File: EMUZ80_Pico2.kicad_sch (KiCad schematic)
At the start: 16 parts, among them J1 Conn_01x20_Socket, J2 Conn_01x20_Socket, SW1 SW_Push, SW2 SW_Push, U1 Pimoroni PGA2350B, U2 RB2350B_Core_Board, U3 74HC00, U4 Z80CPU, U5 HM628128_DIP32_SOP32

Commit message: schematic finished
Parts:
- removed J1, J2: Conn_01x20_Socket, Connector_PinSocket_2.54mm:PinSocket_1x20_P2.54mm_Vertical, symbol kuma-lib1:Conn_01x20_Socket
- removed U3: 74HC00, Package_DIP:DIP-14_W7.62mm_Socket, symbol kuma-lib1:74HC00
- added C1, C2: 0.1u, symbol Device:C_Small
- added C3, C4, C5, C6: C_Small, symbol Device:C_Small
- added D5: D_Schottky_Small, symbol local:D_Schottky_Small
- added J1: Z80_L, symbol local:Conn_01x20_Socket
- added J2: Z80_R, symbol local:Conn_01x20_Socket
- added J3: EXT_GPIO1, symbol Connector:Conn_01x08_Pin
- added J4: EXT_GPIO2, symbol Connector:Conn_01x02_Pin
- added J5: Serial, symbol Connector:Conn_01x06_Pin
- added J6: USB_B_Micro, symbol Connector:USB_B_Micro
- added J8: Conn_01x05_Pin, symbol Connector:Conn_01x05_Pin
- added JP1: VCC_Jumper, symbol Jumper:Jumper_2_Small_Bridged
- added U3: 74HC00, symbol local:74HC00
- D2: value LED_Small -> RED; footprint kuma-f:LED_D3.0mm -> local-f:LED_D3.0mm
- D3: value LED_Small -> GREEN; footprint kuma-f:LED_D3.0mm -> local-f:LED_D3.0mm
- D4: value LED_Small -> YELLOW; footprint kuma-f:LED_D3.0mm -> local-f:LED_D3.0mm
- R1, R2, R3: value R_Small -> 1k; footprint kuma-f:R_Axial_DIN0207_L6.3mm_D2.5mm_P7.62mm_Horizontal -> local-f:R_Axial_DIN0207_L6.3mm_D2.5mm_P7.62mm_Horizontal
- SW1: value SW_Push -> RUN; footprint kuma-f:Tact_SW -> local-f:Tact_SW
- SW2: value SW_Push -> BOOTSEL; footprint kuma-f:Tact_SW -> local-f:Tact_SW
- U2: footprint local-f:RB2350B_Core_Board -> (none)
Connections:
- net A0: now also J2.11 (Pin_11)
- net A1: now also J2.10 (Pin_10)
- net A10: now also J2.1 (Pin_1)
- net A11: now also J1.1 (Pin_1)
- net A12: now also J1.2 (Pin_2)
- net A13: now also J1.3 (Pin_3)
- net A14: now also J1.4 (Pin_4)
- net A15: now also J1.5 (Pin_5)
- net A2: now also J2.9 (Pin_9)
- net A3: now also J2.8 (Pin_8)
- net A4: now also J2.7 (Pin_7)
- net A5: now also J2.6 (Pin_6)
- net A6: now also J2.5 (Pin_5)
- net A7: now also J2.4 (Pin_4)
- net A8: now also J2.3 (Pin_3)
- net A9: now also J2.2 (Pin_2)
- net BUSAK: now also U1.I8 (GPIO29), U2.R25 (GPIO29), J2.18 (Pin_18)
- net BUSRQ: now also U1.C9 (GPIO43_ADC3), U2.R11 (GPIO43_ADC3), J2.16 (Pin_16)
- net CLK: now also J1.6 (Pin_6), U3.11
- net D0: now also J1.14 (Pin_14)
- net D1: now also J1.15 (Pin_15)
- net D2: now also J1.12 (Pin_12)
- net D3: now also J1.8 (Pin_8)
- net D4: now also J1.7 (Pin_7)
- net D5: now also J1.9 (Pin_9)
- net D6: now also J1.10 (Pin_10)
- net D7: now also J1.13 (Pin_13)
- net GND: now also R1.2, SW1.1, SW2.1, U1.A1 (GND), U1.A10 (GND), U1.B2 (GND), U1.B9 (GND), U1.J1 (GND), U1.J10 (GND), U2.L3 (GND), U2.L4 (GND), U2.R1 (GND), U2.R2 (GND), U2.R4 (GND), C1.2, C2.2, C3.2, C4.2, C5.2, C6.2, J2.12 (Pin_12), J5.6 (Pin_6), J6.5 (GND), J6.6 (Shield), J8.5 (Pin_5), U3.7 (GND)
- net HALT: now also R3.2, J1.18 (Pin_18)
- net INT: now also J1.16 (Pin_16), U3.3
- net IORQ: now also U1.J6 (GPIO24), U2.L30 (GPIO24), J1.20 (Pin_20)
- net M1: now also U1.I7 (GPIO27), U2.R27 (GPIO27), J2.14 (Pin_14)
- net MREQ: now also U1.I6 (GPIO25), U2.R29 (GPIO25), J1.19 (Pin_19)
- net NMI: now also J1.17 (Pin_17)
- net RD: now also U1.J7 (GPIO26), U2.R30 (GPIO26), J2.20 (Pin_20)
- net RESET: now also R2.2, U1.D10 (GPIO42_ADC2), U2.R14 (GPIO42_ADC2), J2.15 (Pin_15)
- net RFSH: now also U1.J8 (GPIO28), U2.R28 (GPIO28), J2.13 (Pin_13)
- net VCC: now also D2.2 (A), D3.2 (A), D4.2 (A), U4.11 (VCC), U5.32 (VCC), C1.1, C2.1, J1.11 (Pin_11), JP1.2 (B), U3.13, U3.14 (VCC), U3.2
- net WAIT: now also U1.I9 (GPIO31), U2.R23 (GPIO31), J2.17 (Pin_17)
- net WR: now also U1.J9 (GPIO30), U2.R26 (GPIO30), J2.19 (Pin_19)
- net +5V: now reaches D1.1 (K)
- net +5V: now also U1.A3 (VBUS), C3.1, C4.1, C5.1, C6.1, D5.1 (K), JP1.1 (A)
- net at D1.2 (A): now also J6.1 (VBUS), J8.1 (Pin_1)
- net at D3.1 (K): now also R2.1
- net at R1.1: now also D2.1 (K)
- net RAMCS: now reaches U5.30 (CS2/CE2)
- net RAMCS: now also U1.C10 (GPIO44_ADC4), U2.R12 (GPIO44_ADC4), J4.1 (Pin_1)
- net at D4.1 (K): now also R3.1
- net at U2.L1 (VBUS): now also D5.2 (A)
- net RX: now reaches U2.R10 (GPIO46_ADC6)
- net RX: now also U1.A9 (GPIO46_ADC6), J5.2 (Pin_2)
- net GPIO41: now reaches U2.R13 (GPIO41_ADC1)
- net GPIO41: now also U1.D9 (GPIO41_ADC1), U3.1
- net GPIO39: now reaches U2.R15 (GPIO39)
- net GPIO39: now also U1.E9 (GPIO39), J3.8 (Pin_8)
- net GPIO40: now reaches U2.R16 (GPIO40_ADC0)
- net GPIO40: now also U1.E10 (GPIO40_ADC0), U3.12
- net GPIO37: now reaches U2.R17 (GPIO37)
- net GPIO37: now also U1.F9 (GPIO37), J3.6 (Pin_6)
- net GPIO38: now reaches U2.R18 (GPIO38)
- net GPIO38: now also U1.F10 (GPIO38), J3.7 (Pin_7)
- net GPIO35: now reaches U2.R19 (GPIO35)
- net GPIO35: now also U1.G9 (GPIO35), J3.4 (Pin_4)
- net GPIO36: now reaches U2.R20 (GPIO36)
- net GPIO36: now also U1.G10 (GPIO36), J3.5 (Pin_5)
- net GPIO33: now reaches U2.R21 (GPIO33)
- net GPIO33: now also U1.H9 (GPIO33), J3.2 (Pin_2)
- net GPIO34: now reaches U2.R22 (GPIO34)
- net GPIO34: now also U1.H10 (GPIO34), J3.3 (Pin_3)
- net GPIO32: now reaches U2.R24 (GPIO32)
- net GPIO32: now also U1.I10 (GPIO32), J3.1 (Pin_1)
- net TX: now reaches U2.R7 (GPIO47_ADC7)
- net TX: now also U1.B8 (GPIO47_ADC7), J5.3 (Pin_3)
- net GPIO45: now reaches U2.R9 (GPIO45_ADC5)
- net GPIO45: now also U1.B10 (GPIO45_ADC5), J4.2 (Pin_2)
- net at U1.A5 (RUN): now also SW1.2
- net at U1.A6 (USB_DP): now also J6.3 (D+), J8.3 (Pin_3)
- net at U1.A7 (USB_DM): now also J6.2 (D-), J8.2 (Pin_2)
- net at U1.A8 (BOOTSEL): now also SW2.2
- new net CTS: J5.5 (Pin_5)
- new net DTR: J5.1 (Pin_1)
- no-connect marks 0 -> 22
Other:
- note added: "D+"
- note added: "D-"
- note added: "GND"
- note added: "ID"
- note added: "VCC"
- moved on the sheet: D1, D2, D3, D4, R1, R2, R3, SW1, SW2

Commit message: schematic done, pcb now working
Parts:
- removed C6: C_Small, symbol Device:C_Small
- added C7: 10uF, Capacitor_THT:CP_Radial_D5.0mm_P2.50mm, symbol Device:C_Polarized_Small
- C1, C2: footprint (none) -> Capacitor_THT:C_Disc_D3.0mm_W1.6mm_P2.50mm
- C3, C4, C5: value C_Small -> 0.1u; footprint (none) -> Capacitor_THT:C_Disc_D3.0mm_W1.6mm_P2.50mm
- D1, D5: value D_Schottky_Small -> 1S3; footprint (none) -> local-f:D_DO-34_SOD68_P7.62mm_Horizontal
- J1, J2: footprint (none) -> local-f:PinHeader_1x20_P2.54mm_Ovalpad_Vertical
- J3: footprint (none) -> Connector_PinHeader_2.54mm:PinHeader_1x08_P2.54mm_Vertical
- J4: footprint (none) -> Connector_PinHeader_2.54mm:PinHeader_1x02_P2.54mm_Vertical
- J5: footprint (none) -> local-f:PinHeader_1x06_P2.54mm_Horizontal_NoFeet
- J6: footprint (none) -> Connector_USB:USB_Micro-B_Amphenol_10103594-0001LF_Horizontal
- J8: footprint (none) -> Connector_PinHeader_2.54mm:PinHeader_1x05_P2.54mm_Vertical
- JP1: footprint (none) -> Jumper:SolderJumper-2_P1.3mm_Bridged_RoundedPad1.0x1.5mm
- R1, R2, R3: footprint local-f:R_Axial_DIN0207_L6.3mm_D2.5mm_P7.62mm_Horizontal -> local-f:R_Axial_L5.5mm_D2.0mm_P7.62mm_Horizontal
- U2: footprint (none) -> local-f:RB2350B_Core_Board
- U3: footprint (none) -> Package_DIP:DIP-14_W7.62mm_Socket
- U4: footprint Package_DIP:DIP-40_W15.24mm_Socket -> local-f:DIP-40_W15.24mm_Socket_OvalPad_splitcouryard
- U5: value HM628128_DIP32_SOP32 -> HM628128
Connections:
- net +5V: now also D2.2 (A), C7.1; no longer C3.1
- net GND: now also C7.2; no longer C3.2
- net VCC: now also C3.1; no longer D2.2 (A)
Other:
- moved on the sheet: C3, C4, C5, D2, R1

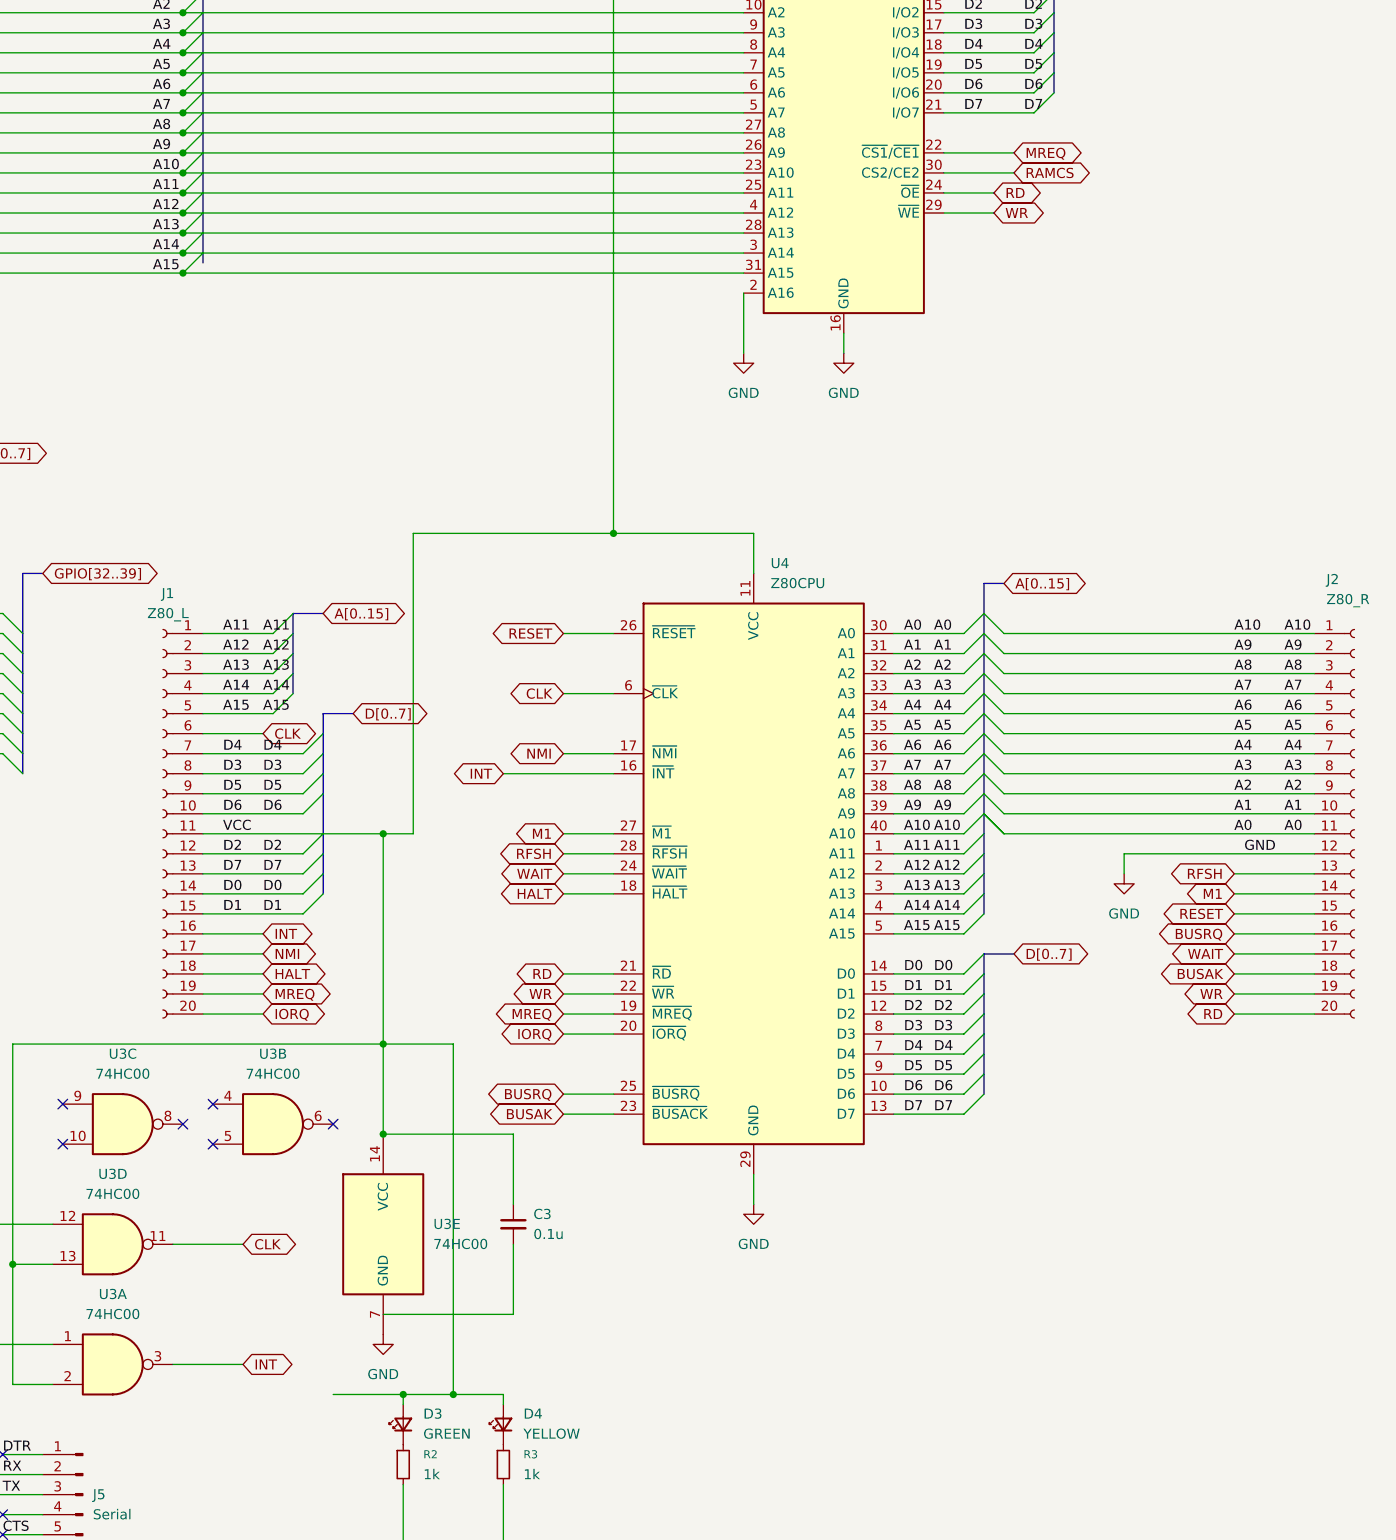
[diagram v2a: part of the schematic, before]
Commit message: EMUZ80_Pico2: PCB routing completed, ready to order
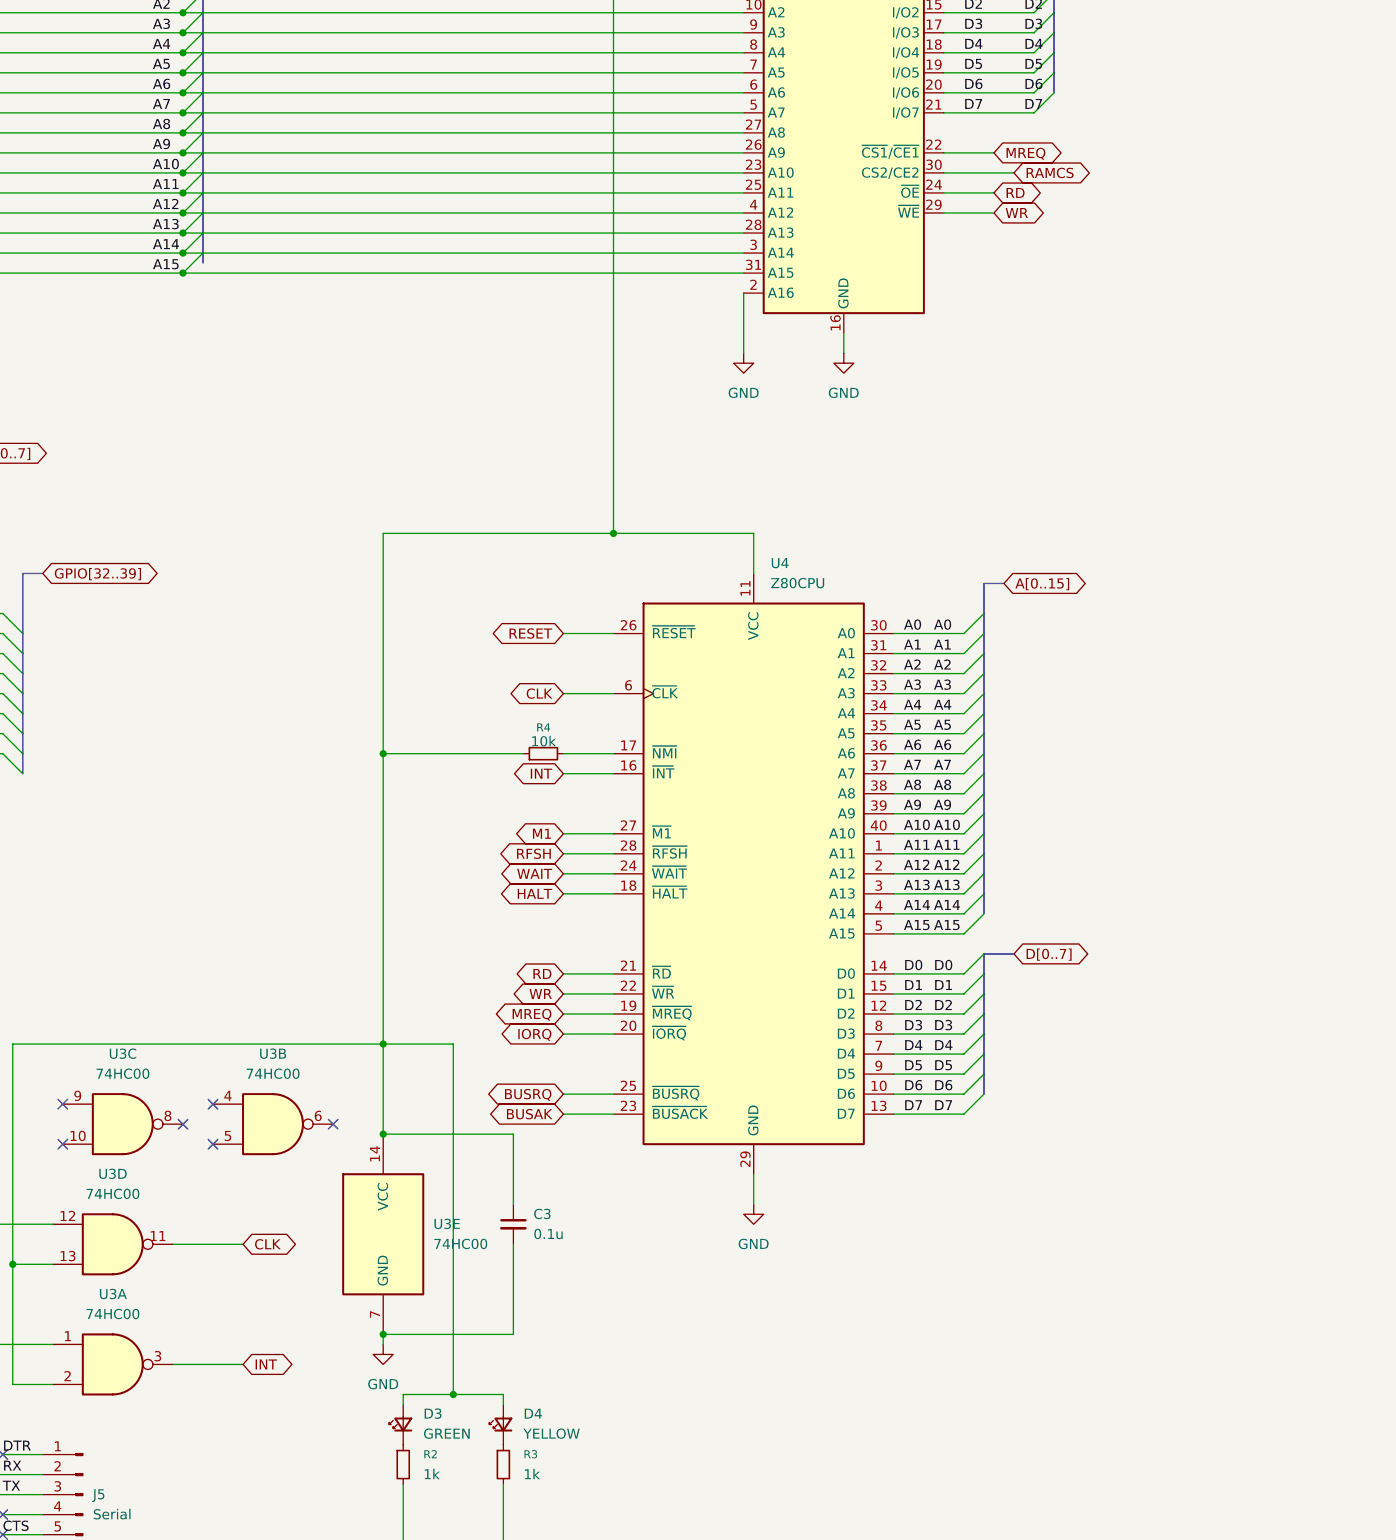
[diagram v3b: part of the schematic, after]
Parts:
- removed J1: Z80_L, local-f:PinHeader_1x20_P2.54mm_Ovalpad_Vertical, symbol local:Conn_01x20_Socket
- removed J2: Z80_R, local-f:PinHeader_1x20_P2.54mm_Ovalpad_Vertical, symbol local:Conn_01x20_Socket
- added R4: 10k, local-f:R_Axial_L5.5mm_D2.0mm_P7.62mm_Horizontal, symbol local:R_Small
- U4: footprint local-f:DIP-40_W15.24mm_Socket_OvalPad_splitcouryard -> local-f:DIP-40_SidePin_Z80
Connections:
- net GND: now also C3.2
- net NMI: no longer names the net of U4.17 (~{NMI})
- net NMI: now also R4.2
- net VCC: no longer names the net of C1.1, C2.1, C3.1, D3.2 (A), D4.2 (A), JP1.2 (B), U3.13, U3.14 (VCC), U3.2, U4.11 (VCC), U5.32 (VCC)
- net VCC: now also R4.1

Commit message: PCB rev001 finished, ready to order JLCPCB
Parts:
- U5: footprint Package_DIP:DIP-32_W15.24mm_Socket -> local-f:DIP-32_W15.24mm_OvalPads
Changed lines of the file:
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@@
 			)
 		)
-		(property "Footprint" "Package_DIP:DIP-32_W15.24mm_Socket"
+		(property "Footprint" "local-f:DIP-32_W15.24mm_OvalPads"
 			(at 325.12 82.55 0)
 			(effects

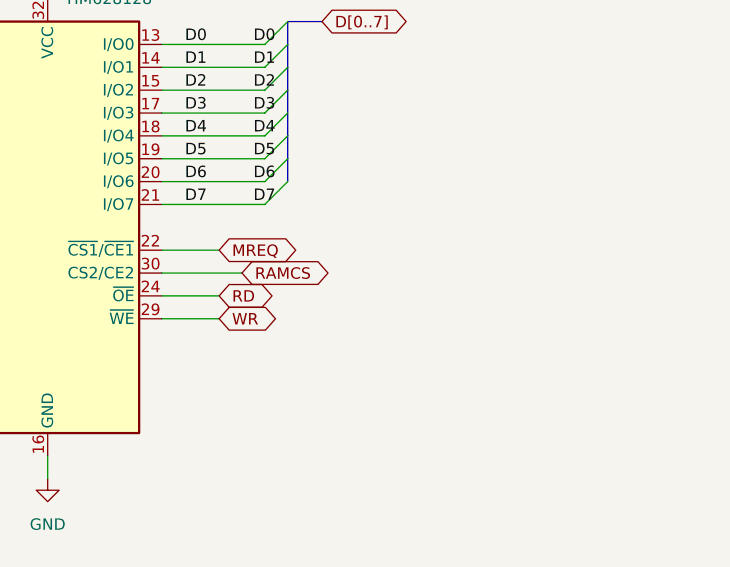
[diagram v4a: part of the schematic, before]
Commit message: add JP2-5 to SRAM Controls
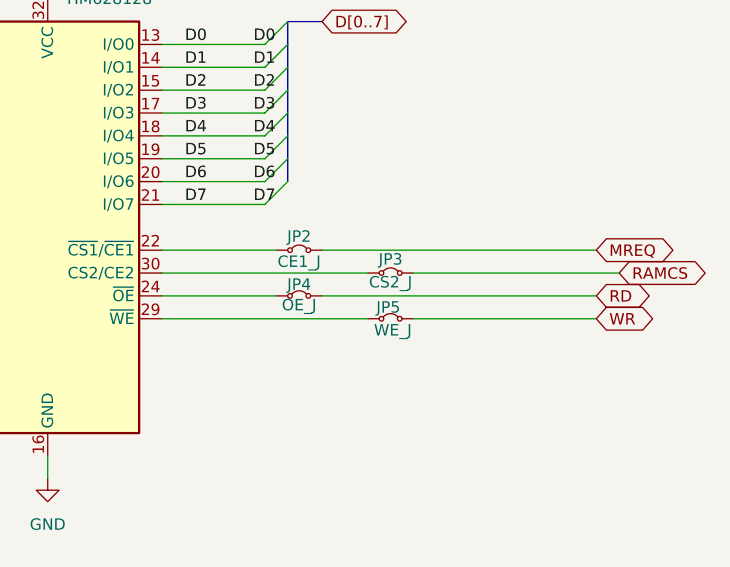
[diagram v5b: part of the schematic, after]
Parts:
- added JP2: CE1_J, Jumper:SolderJumper-2_P1.3mm_Bridged_RoundedPad1.0x1.5mm, symbol Jumper:Jumper_2_Small_Bridged
- added JP3: CS2_J, Jumper:SolderJumper-2_P1.3mm_Bridged_RoundedPad1.0x1.5mm, symbol Jumper:Jumper_2_Small_Bridged
- added JP4: OE_J, Jumper:SolderJumper-2_P1.3mm_Bridged_RoundedPad1.0x1.5mm, symbol Jumper:Jumper_2_Small_Bridged
- added JP5: WE_J, Jumper:SolderJumper-2_P1.3mm_Bridged_RoundedPad1.0x1.5mm, symbol Jumper:Jumper_2_Small_Bridged
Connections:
- net MREQ: now also JP2.2 (B); no longer U5.22 (~{CS1}/~{CE1})
- net RAMCS: now also JP3.2 (B); no longer U5.30 (CS2/CE2)
- net RD: now also JP4.2 (B); no longer U5.24 (~{OE})
- net WR: now also JP5.2 (B); no longer U5.29 (~{WE})
- new net: JP2.1 (A), U5.22 (~{CS1}/~{CE1})
- new net: JP5.1 (A), U5.29 (~{WE})
- new net: JP4.1 (A), U5.24 (~{OE})
- new net: JP3.1 (A), U5.30 (CS2/CE2)

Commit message: Rev001: order data
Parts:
- J6: footprint Connector_USB:USB_Micro-B_Amphenol_10103594-0001LF_Horizontal -> local-f:USB_Micro-B_Hirose_ZX62-B-5PA
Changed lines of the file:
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@@
 			)
 		)
-		(property "Footprint" "Connector_USB:USB_Micro-B_Amphenol_10103594-0001LF_Horizontal"
+		(property "Footprint" "local-f:USB_Micro-B_Hirose_ZX62-B-5PA"
 			(at 107.95 26.67 0)
 			(effects
